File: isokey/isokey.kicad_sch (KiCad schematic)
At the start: 69 parts, among them J1 PadExp Left, J2 PadExp Right, Q1 BSS138, SW73 RotaryEncoder_Switch, SW74 RotaryEncoder_Switch, U1 BlackPill_STLINK, U4 TLV73318PDBV

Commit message: Complete routing
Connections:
- net c14 is gone; now on net cl14: J1.10 (Pin_10), J2.10 (Pin_10)
- net c15 is gone; now on net cl15: J1.11 (Pin_11), J2.11 (Pin_11)
- net cl0: now also R17.1; no longer R17.1
- net cl1: now also R17.1; no longer R17.1
- net cl10: now also R17.1; no longer R17.1
- net cl11: now also R17.1; no longer R17.1
- net cl12: now also R17.1; no longer R17.1
- net cl13: now also R17.1; no longer R17.1
- net cl14: now also R17.1; no longer R17.1
- net cl15: now also R17.1; no longer R17.1
- net cl16: now also R17.1; no longer R17.1
- net cl17: now also R17.1; no longer R17.1
- net cl2: now also R17.1; no longer R17.1
- net cl3: now also R17.1; no longer R17.1
- net cl4: now also R17.1; no longer R17.1
- net cl5: now also R17.1; no longer R17.1
- net cl6: now also R17.1; no longer R17.1
- net cl7: now also R17.1; no longer R17.1
- net cl8: now also R17.1; no longer R17.1
- net cl9: now also R17.1; no longer R17.1
- net r-1: now also R17.1; no longer R17.1
- net r0: now also R17.1; no longer R17.1
- net r1: now also R17.1; no longer R17.1
- net r2: now also R17.1; no longer R17.1
- net r3: now also R17.1; no longer R17.1
- net r4: now also R17.1; no longer R17.1
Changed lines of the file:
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@@
     (effects (font (size 1.27 1.27)) (justify left bottom))
   )
-  (label "cl12" (at 106.68 66.04 0) (fields_autoplaced)
+  (label "cl12" (at 179.705 35.56 0) (fields_autoplaced)
     (effects (font (size 1.27 1.27)) (justify left bottom))
   )
@@
     (effects (font (size 1.27 1.27)) (justify right bottom))
   )
-  (label "cl16" (at 106.68 77.47 0) (fields_autoplaced)
+  (label "cl16" (at 176.53 45.72 0) (fields_autoplaced)
     (effects (font (size 1.27 1.27)) (justify left bottom))
   )
@@
     (effects (font (size 1.27 1.27)) (justify left bottom))
   )
-  (label "c15" (at 40.005 43.18 180) (fields_autoplaced)
-    (effects (font (size 1.27 1.27)) (justify right bottom))
-  )
-  (label "cl14" (at 106.68 71.12 0) (fields_autoplaced)
+  (label "cl15" (at 40.005 43.18 180) (fields_autoplaced)
+    (effects (font (size 1.27 1.27)) (justify right bottom))
+  )
+  (label "cl14" (at 180.34 60.96 0) (fields_autoplaced)
     (effects (font (size 1.27 1.27)) (justify left bottom))
   )
@@
     (effects (font (size 1.27 1.27)) (justify left bottom))
   )
-  (label "c14" (at 40.005 40.64 180) (fields_autoplaced)
+  (label "cl14" (at 40.005 40.64 180) (fields_autoplaced)
     (effects (font (size 1.27 1.27)) (justify right bottom))
   )
@@
     (effects (font (size 1.27 1.27)) (justify right bottom))
   )
-  (label "r0" (at 106.68 38.1 0) (fields_autoplaced)
+  (label "r0" (at 107.315 58.42 0) (fields_autoplaced)
     (effects (font (size 1.27 1.27)) (justify left bottom))
   )
@@
     (effects (font (size 1.27 1.27)) (justify left bottom))
   )
-  (label "cl5" (at 177.165 58.42 0) (fields_autoplaced)
-    (effects (font (size 1.27 1.27)) (justify left bottom))
-  )
-  (label "c15" (at 260.35 41.91 0) (fields_autoplaced)
-    (effects (font (size 1.27 1.27)) (justify left bottom))
-  )
-  (label "r-1" (at 106.68 50.8 0) (fields_autoplaced)
+  (label "cl5" (at 106.68 40.64 0) (fields_autoplaced)
+    (effects (font (size 1.27 1.27)) (justify left bottom))
+  )
+  (label "cl15" (at 260.35 41.91 0) (fields_autoplaced)
+    (effects (font (size 1.27 1.27)) (justify left bottom))
+  )
+  (label "r-1" (at 107.315 71.12 0) (fields_autoplaced)
     (effects (font (size 1.27 1.27)) (justify left bottom))
   )
@@
     (effects (font (size 1.27 1.27)) (justify left bottom))
   )
-  (label "c14" (at 260.35 39.37 0) (fields_autoplaced)
+  (label "cl14" (at 260.35 39.37 0) (fields_autoplaced)
     (effects (font (size 1.27 1.27)) (justify left bottom))
   )
@@
     (effects (font (size 1.27 1.27)) (justify left bottom))
   )
-  (label "cl0" (at 176.53 35.56 0) (fields_autoplaced)
+  (label "cl0" (at 177.8 55.88 0) (fields_autoplaced)
     (effects (font (size 1.27 1.27)) (justify left bottom))
   )
@@
     (effects (font (size 1.27 1.27)) (justify left bottom))
   )
-  (label "cl8" (at 107.315 55.88 0) (fields_autoplaced)
+  (label "cl8" (at 106.68 48.26 0) (fields_autoplaced)
     (effects (font (size 1.27 1.27)) (justify left bottom))
   )
@@
     (effects (font (size 1.27 1.27)) (justify left bottom))
   )
-  (label "r1" (at 106.68 40.64 0) (fields_autoplaced)
+  (label "r1" (at 107.315 60.96 0) (fields_autoplaced)
     (effects (font (size 1.27 1.27)) (justify left bottom))
   )
@@
     (effects (font (size 1.27 1.27)) (justify left bottom))
   )
-  (label "cl4" (at 177.165 55.88 0) (fields_autoplaced)
+  (label "cl4" (at 106.68 38.1 0) (fields_autoplaced)
     (effects (font (size 1.27 1.27)) (justify left bottom))
   )
@@
     (effects (font (size 1.27 1.27)) (justify left bottom))
   )
-  (label "cl1" (at 176.53 38.1 0) (fields_autoplaced)
-    (effects (font (size 1.27 1.27)) (justify left bottom))
-  )
-  (label "r3" (at 106.68 45.72 0) (fields_autoplaced)
-    (effects (font (size 1.27 1.27)) (justify left bottom))
-  )
-  (label "cl15" (at 106.68 74.93 0) (fields_autoplaced)
-    (effects (font (size 1.27 1.27)) (justify left bottom))
-  )
-  (label "cl11" (at 106.68 63.5 0) (fields_autoplaced)
-    (effects (font (size 1.27 1.27)) (justify left bottom))
-  )
-  (label "cl7" (at 107.315 53.34 0) (fields_autoplaced)
+  (label "cl1" (at 106.68 74.93 0) (fields_autoplaced)
+    (effects (font (size 1.27 1.27)) (justify left bottom))
+  )
+  (label "r3" (at 107.315 66.04 0) (fields_autoplaced)
+    (effects (font (size 1.27 1.27)) (justify left bottom))
+  )
+  (label "cl15" (at 176.53 48.26 0) (fields_autoplaced)
+    (effects (font (size 1.27 1.27)) (justify left bottom))
+  )
+  (label "cl11" (at 106.68 55.88 0) (fields_autoplaced)
+    (effects (font (size 1.27 1.27)) (justify left bottom))
+  )
+  (label "cl7" (at 106.68 45.72 0) (fields_autoplaced)
     (effects (font (size 1.27 1.27)) (justify left bottom))
   )
@@
     (effects (font (size 1.27 1.27)) (justify left bottom))
   )
-  (label "cl6" (at 177.165 60.96 0) (fields_autoplaced)
+  (label "cl6" (at 106.68 43.18 0) (fields_autoplaced)
     (effects (font (size 1.27 1.27)) (justify left bottom))
   )
@@
     (effects (font (size 1.27 1.27)) (justify left bottom))
   )
-  (label "cl3" (at 176.53 48.26 0) (fields_autoplaced)
-    (effects (font (size 1.27 1.27)) (justify left bottom))
-  )
-  (label "r4" (at 106.68 48.26 0) (fields_autoplaced)
+  (label "cl3" (at 106.68 80.01 0) (fields_autoplaced)
+    (effects (font (size 1.27 1.27)) (justify left bottom))
+  )
+  (label "r4" (at 107.315 68.58 0) (fields_autoplaced)
     (effects (font (size 1.27 1.27)) (justify left bottom))
   )
@@
     (effects (font (size 1.27 1.27)) (justify left bottom))
   )
-  (label "cl13" (at 106.68 68.58 0) (fields_autoplaced)
+  (label "cl13" (at 179.705 38.1 0) (fields_autoplaced)
     (effects (font (size 1.27 1.27)) (justify left bottom))
   )
@@
     (effects (font (size 1.27 1.27)) (justify left bottom))
   )
-  (label "r2" (at 106.68 43.18 0) (fields_autoplaced)
+  (label "r2" (at 107.315 63.5 0) (fields_autoplaced)
     (effects (font (size 1.27 1.27)) (justify left bottom))
   )
@@
     (effects (font (size 1.27 1.27)) (justify left bottom))
   )
-  (label "cl10" (at 106.68 60.96 0) (fields_autoplaced)
+  (label "cl10" (at 106.68 53.34 0) (fields_autoplaced)
     (effects (font (size 1.27 1.27)) (justify left bottom))
   )
@@
     (effects (font (size 1.27 1.27)) (justify left bottom))
   )
-  (label "cl17" (at 106.68 80.01 0) (fields_autoplaced)
-    (effects (font (size 1.27 1.27)) (justify left bottom))
-  )
-  (label "cl9" (at 106.68 58.42 0) (fields_autoplaced)
+  (label "cl17" (at 180.34 58.42 0) (fields_autoplaced)
+    (effects (font (size 1.27 1.27)) (justify left bottom))
+  )
+  (label "cl9" (at 106.68 50.8 0) (fields_autoplaced)
     (effects (font (size 1.27 1.27)) (justify left bottom))
   )
@@
     (effects (font (size 1.27 1.27)) (justify left bottom))
   )
-  (label "cl2" (at 176.53 45.72 0) (fields_autoplaced)
-    (effects (font (size 1.27 1.27)) (justify left bottom))
-  )
+  (label "cl2" (at 106.68 77.47 0) (fields_autoplaced)
+    (effects (font (size 1.27 1.27)) (justify left bottom))
+  )

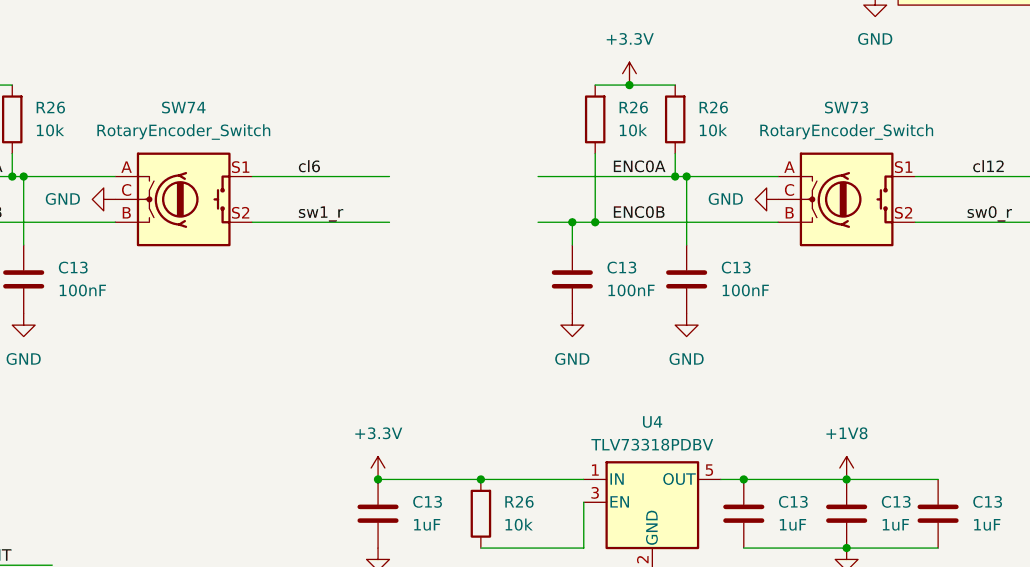
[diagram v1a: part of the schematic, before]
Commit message: complete routing
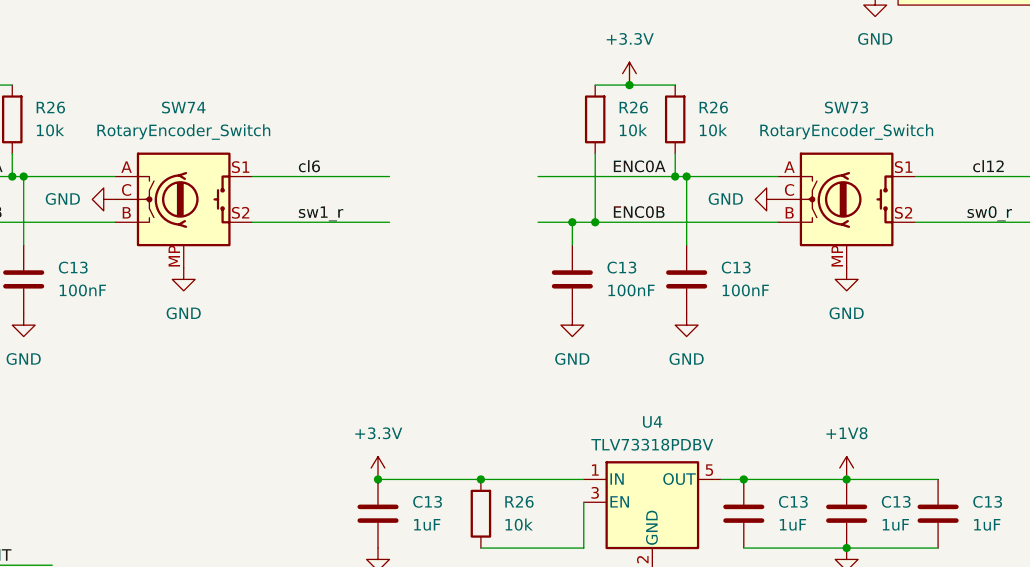
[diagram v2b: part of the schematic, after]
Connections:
- net GND: now also SW73.MP, SW74.MP
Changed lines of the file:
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@@
     (pin "B")
     (pin "C")
+    (pin "MP")
     (pin "S1")
     (pin "S2")
@@
         (path "/b0c352a4-2db1-45ff-8668-f2efdeb7d408"
           (reference "R18") (unit 1)
+        )
+      )
+    )
+  )
+  (symbol (lib_id "power:GND") (at 159.385 126.365 0) (unit 1)
+    (in_bom yes) (on_board yes) (dnp no) (fields_autoplaced)
+    (property "Reference" "#PWR0246" (at 159.385 132.715 0)
+      (effects (font (size 1.27 1.27)) hide)
+    )
+    (property "Value" "GND" (at 159.385 131.445 0)
+      (effects (font (size 1.27 1.27)))
+    )
+    (property "Footprint" "" (at 159.385 126.365 0)
+      (effects (font (size 1.27 1.27)) hide)
+    )
+    (property "Datasheet" "" (at 159.385 126.365 0)
+      (effects (font (size 1.27 1.27)) hide)
+    )
+    (pin "1")
+    (instances
+      (project "isokey"
+        (path "/b0c352a4-2db1-45ff-8668-f2efdeb7d408/08b818ec-1371-4ecd-bb59-e4167af93fdf"
+          (reference "#PWR0246") (unit 1)
+        )
+        (path "/b0c352a4-2db1-45ff-8668-f2efdeb7d408"
+          (reference "#PWR0217") (unit 1)
         )
       )
@@
     (pin "B")
     (pin "C")
+    (pin "MP")
     (pin "S1")
     (pin "S2")
@@
         )
       )
+    )
+  )
+  (symbol (lib_id "power:GND") (at 233.045 126.365 0) (unit 1)
+    (in_bom yes) (on_board yes) (dnp no) (fields_autoplaced)
+    (property "Reference" "#PWR0246" (at 233.045 132.715 0)
+      (effects (font (size 1.27 1.27)) hide)
+    )
+    (property "Value" "GND" (at 233.045 131.445 0)
+      (effects (font (size 1.27 1.27)))
+    )
+    (property "Footprint" "" (at 233.045 126.365 0)
+      (effects (font (size 1.27 1.27)) hide)
+    )
+    (property "Datasheet" "" (at 233.045 126.365 0)
+      (effects (font (size 1.27 1.27)) hide)
+    )
+    (pin "1")
+    (instances
+      (project "isokey"
+        (path "/b0c352a4-2db1-45ff-8668-f2efdeb7d408/08b818ec-1371-4ecd-bb59-e4167af93fdf"
+          (reference "#PWR0246") (unit 1)
+        )
+        (path "/b0c352a4-2db1-45ff-8668-f2efdeb7d408"
+          (reference "#PWR0221") (unit 1)
+        )
+      )

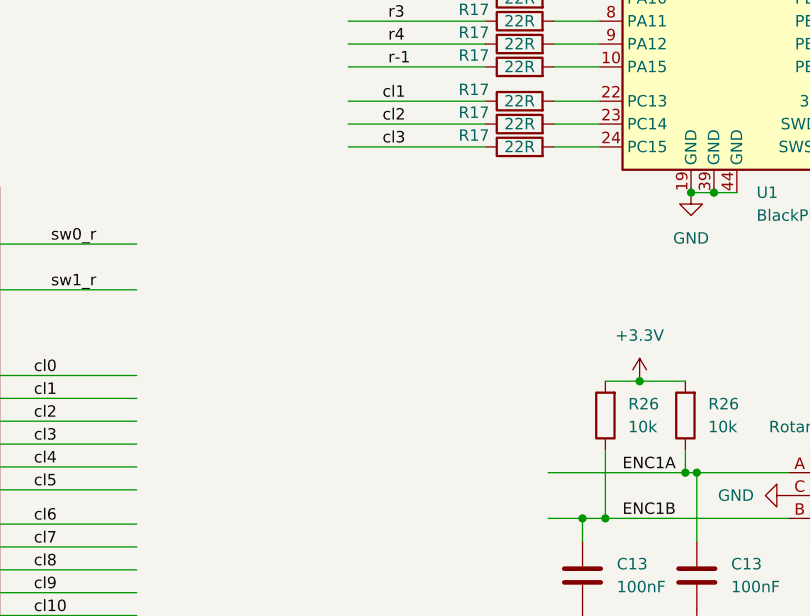
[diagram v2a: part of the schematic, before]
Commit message: Add trackball scheme
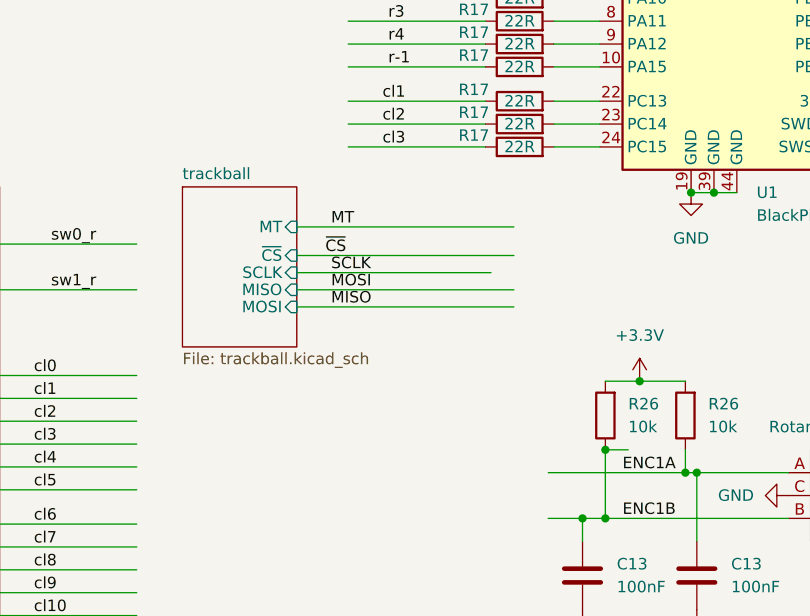
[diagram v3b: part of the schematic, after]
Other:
- added sheet trackball (trackball.kicad_sch)
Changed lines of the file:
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@@
   (junction (at 128.905 121.285) (diameter 0) (color 0 0 0 0)
   )
+  (junction (at 131.445 113.665) (diameter 0) (color 0 0 0 0)
+  )
   (junction (at 144.78 22.86) (diameter 0) (color 0 0 0 0)
   )
@@
     (stroke (width 0) (type default))
   )
+  (wire (pts (xy 97.155 95.885) (xy 121.285 95.885))
+    (stroke (width 0) (type default))
+  )
   (wire (pts (xy 172.72 48.26) (xy 187.96 48.26))
     (stroke (width 0) (type default))
@@
     (stroke (width 0) (type default))
   )
+  (wire (pts (xy 97.155 97.79) (xy 121.285 97.79))
+    (stroke (width 0) (type default))
+  )
   (wire (pts (xy 125.73 71.12) (xy 130.81 71.12))
     (stroke (width 0) (type default))
@@
     (stroke (width 0) (type default))
   )
+  (wire (pts (xy 97.155 93.98) (xy 118.745 93.98))
+    (stroke (width 0) (type default))
+  )
   (wire (pts (xy 240.665 116.205) (xy 255.905 116.205))
     (stroke (width 0) (type default))
@@
     (stroke (width 0) (type default))
   )
+  (wire (pts (xy 97.155 88.9) (xy 121.285 88.9))
+    (stroke (width 0) (type default))
+  )
   (wire (pts (xy 274.32 49.53) (xy 259.08 49.53))
     (stroke (width 0) (type default))
@@
     (stroke (width 0) (type default))
   )
+  (wire (pts (xy 131.445 113.665) (xy 133.985 113.665))
+    (stroke (width 0) (type default))
+  )
   (wire (pts (xy 131.445 121.285) (xy 151.765 121.285))
     (stroke (width 0) (type default))
@@
     (stroke (width 0) (type default))
   )
+  (wire (pts (xy 97.155 92.075) (xy 121.285 92.075))
+    (stroke (width 0) (type default))
+  )
   (wire (pts (xy 233.045 149.86) (xy 243.205 149.86))
     (stroke (width 0) (type default))
@@
     (effects (font (size 1.27 1.27)) (justify left bottom))
   )
+  (label "MISO" (at 100.965 97.79 0) (fields_autoplaced)
+    (effects (font (size 1.27 1.27)) (justify left bottom))
+  )
   (label "r1" (at 36.195 107.95 0) (fields_autoplaced)
     (effects (font (size 1.27 1.27)) (justify left bottom))
@@
     (effects (font (size 1.27 1.27)) (justify right bottom))
   )
+  (label "MT" (at 100.965 88.9 0) (fields_autoplaced)
+    (effects (font (size 1.27 1.27)) (justify left bottom))
+  )
   (label "cl16" (at 176.53 45.72 0) (fields_autoplaced)
     (effects (font (size 1.27 1.27)) (justify left bottom))
@@
     (effects (font (size 1.27 1.27)) (justify left bottom))
   )
+  (label "SCLK" (at 100.965 93.98 0) (fields_autoplaced)
+    (effects (font (size 1.27 1.27)) (justify left bottom))
+  )
   (label "cl11" (at 106.68 55.88 0) (fields_autoplaced)
     (effects (font (size 1.27 1.27)) (justify left bottom))
@@
     (effects (font (size 1.27 1.27)) (justify left bottom))
   )
+  (label "~{CS}" (at 100.33 92.075 0) (fields_autoplaced)
+    (effects (font (size 1.27 1.27)) (justify left bottom))
+  )
   (label "cl0" (at 67.945 105.41 0) (fields_autoplaced)
     (effects (font (size 1.27 1.27)) (justify left bottom))
@@
     (effects (font (size 1.27 1.27)) (justify left bottom))
   )
+  (label "MOSI" (at 100.965 95.885 0) (fields_autoplaced)
+    (effects (font (size 1.27 1.27)) (justify left bottom))
+  )
   (label "sw1_r" (at 69.85 95.885 0) (fields_autoplaced)
     (effects (font (size 1.27 1.27)) (justify left bottom))
@@
       )
     )
+  )
+  (sheet (at 84.455 84.455) (size 12.7 17.78) (fields_autoplaced)
+    (stroke (width 0.1524) (type solid))
+    (fill (color 0 0 0 0.0000))
+    (property "Sheetname" "trackball" (at 84.455 83.7434 0)
+      (effects (font (size 1.27 1.27)) (justify left bottom))
+    )
+    (property "Sheetfile" "trackball.kicad_sch" (at 84.455 102.8196 0)
+      (effects (font (size 1.27 1.27)) (justify left top))
+    )
+    (pin "MT" input (at 97.155 88.9 0)
+      (effects (font (size 1.27 1.27)) (justify right))
+    )
+    (pin "~{CS}" input (at 97.155 92.075 0)
+      (effects (font (size 1.27 1.27)) (justify right))
+    )
+    (pin "SCLK" input (at 97.155 93.98 0)
+      (effects (font (size 1.27 1.27)) (justify right))
+    )
+    (pin "MISO" input (at 97.155 95.885 0)
+      (effects (font (size 1.27 1.27)) (justify right))
+    )
+    (pin "MOSI" input (at 97.155 97.79 0)
+      (effects (font (size 1.27 1.27)) (justify right))
+    )
+    (instances
+      (project "isokey"
+        (path "/b0c352a4-2db1-45ff-8668-f2efdeb7d408" (page "5"))
+      )
+    )
